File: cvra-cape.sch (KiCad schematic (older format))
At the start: 16 parts

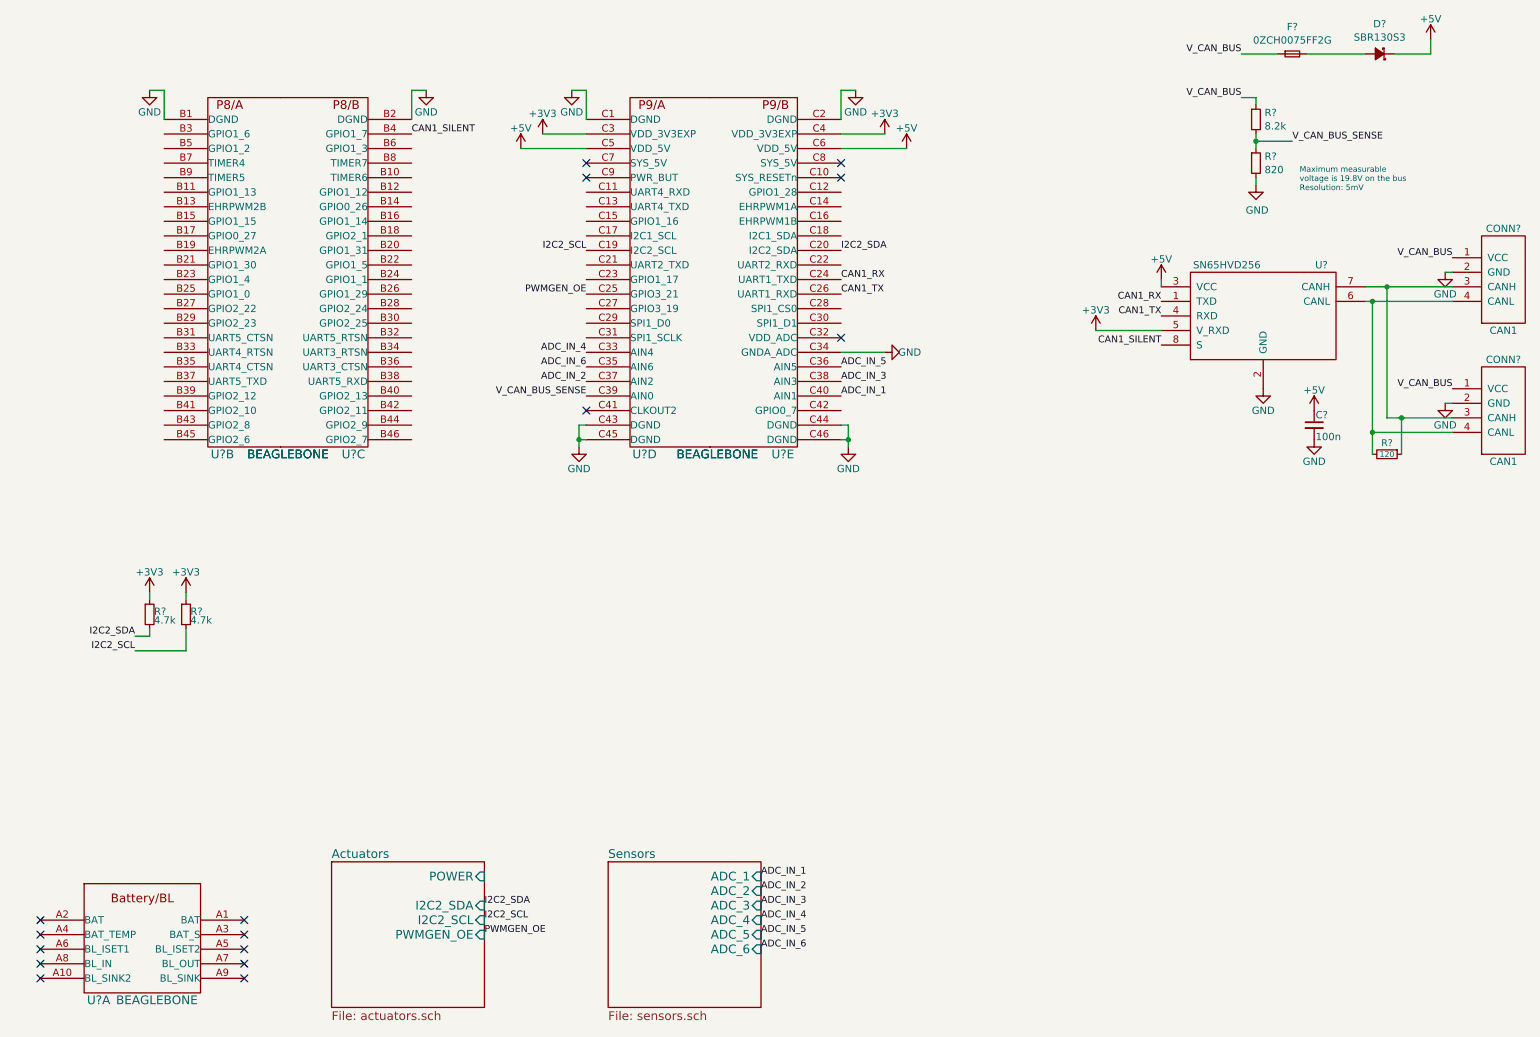
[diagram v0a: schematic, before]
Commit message: Add CAN over SPI interface using MCP251
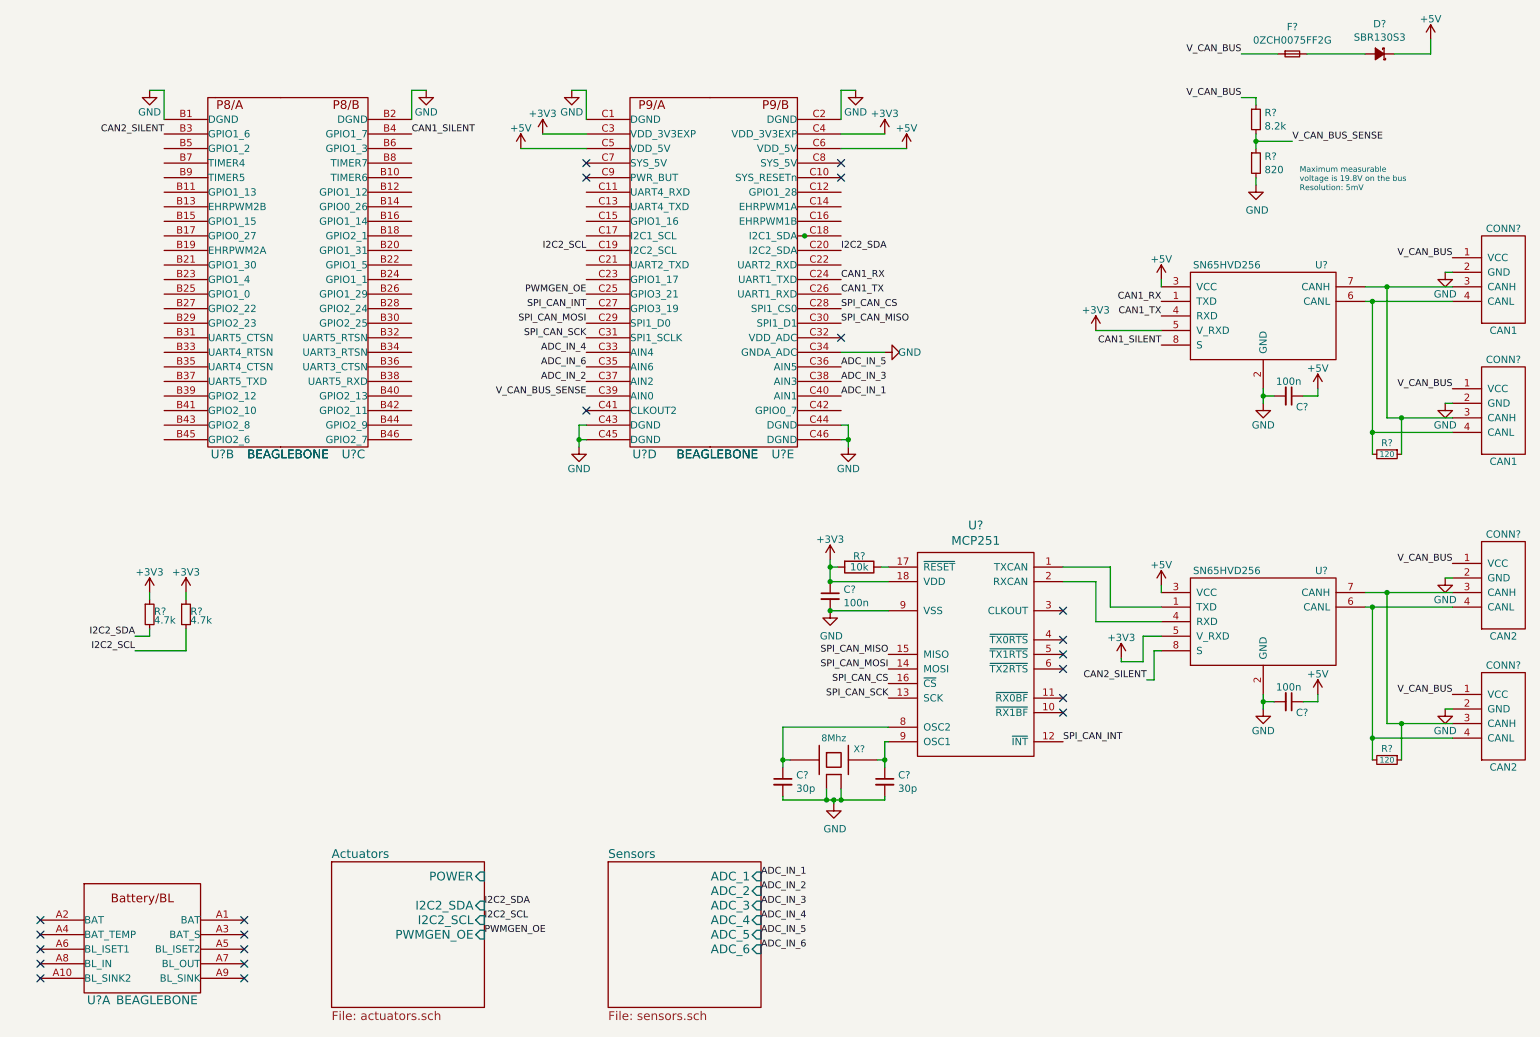
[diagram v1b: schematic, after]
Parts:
- added C? (x2): 30p, symbol C_Small
- added C? (x2): 100n, symbol C_Small
- added CONN? (x2): CAN2, MODULE, symbol CAN
- added R?: 120, symbol R_Small
- added R?: 10k, symbol R
- added U?: SN65HVD256, MODULE, symbol SN65HVD256
- added U?: MCP251, symbol MCP251
- added X?: 8Mhz, symbol XTAL-SMD-4-PADS
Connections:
- net +3V3: now also C?.1, R?.2, U?.18 (VDD), U?.5 (V_RXD)
- net +5V: now also C?.1, U?.3 (VCC)
- net GND: now also C?.2, C?.2, C?.2, C?.2, CONN?.2 (GND), CONN?.2 (GND), CONN?.MECH (GND), CONN?.MECH (GND), U?.2 (GND), U?.9 (VSS), X?.2 (case), X?.4 (case)
- net V_CAN_BUS: now also CONN?.1 (VCC), CONN?.1 (VCC)
- net CAN2_SILENT: now reaches U?.B3 (GPIO1_6)
- net CAN2_SILENT: now also U?.8 (S)
- net SPI_CAN_INT: now reaches U?.C27 (GPIO3_19)
- net SPI_CAN_INT: now also U?.12 (~INT)
- net SPI_CAN_MOSI: now reaches U?.C29 (SPI1_D0)
- net SPI_CAN_MOSI: now also U?.14 (MOSI)
- net SPI_CAN_SCK: now reaches U?.C31 (SPI1_SCLK)
- net SPI_CAN_SCK: now also U?.13 (SCK)
- net SPI_CAN_CS: now reaches U?.C28 (SPI1_CS0)
- net SPI_CAN_CS: now also U?.16 (~CS)
- net SPI_CAN_MISO: now reaches U?.C30 (SPI1_D1)
- net SPI_CAN_MISO: now also U?.15 (MISO)
- new net: U?.1 (TXCAN), U?.1 (TXD)
- new net: U?.2 (RXCAN), U?.4 (RXD)
- new net: CONN?.4 (CANL), CONN?.4 (CANL), R?.2, U?.6 (CANL)
- new net: CONN?.3 (CANH), CONN?.3 (CANH), R?.1, U?.7 (CANH)
- new net: R?.1, U?.17 (~RESET)
- new net: C?.1, U?.8 (OSC2), X?.1
- new net: C?.1, U?.9 (VSS), X?.3
- no-connect marks 16 -> 22
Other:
- moved on the sheet: C?

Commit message: Use 3pin connectors for ADC (with power pin)
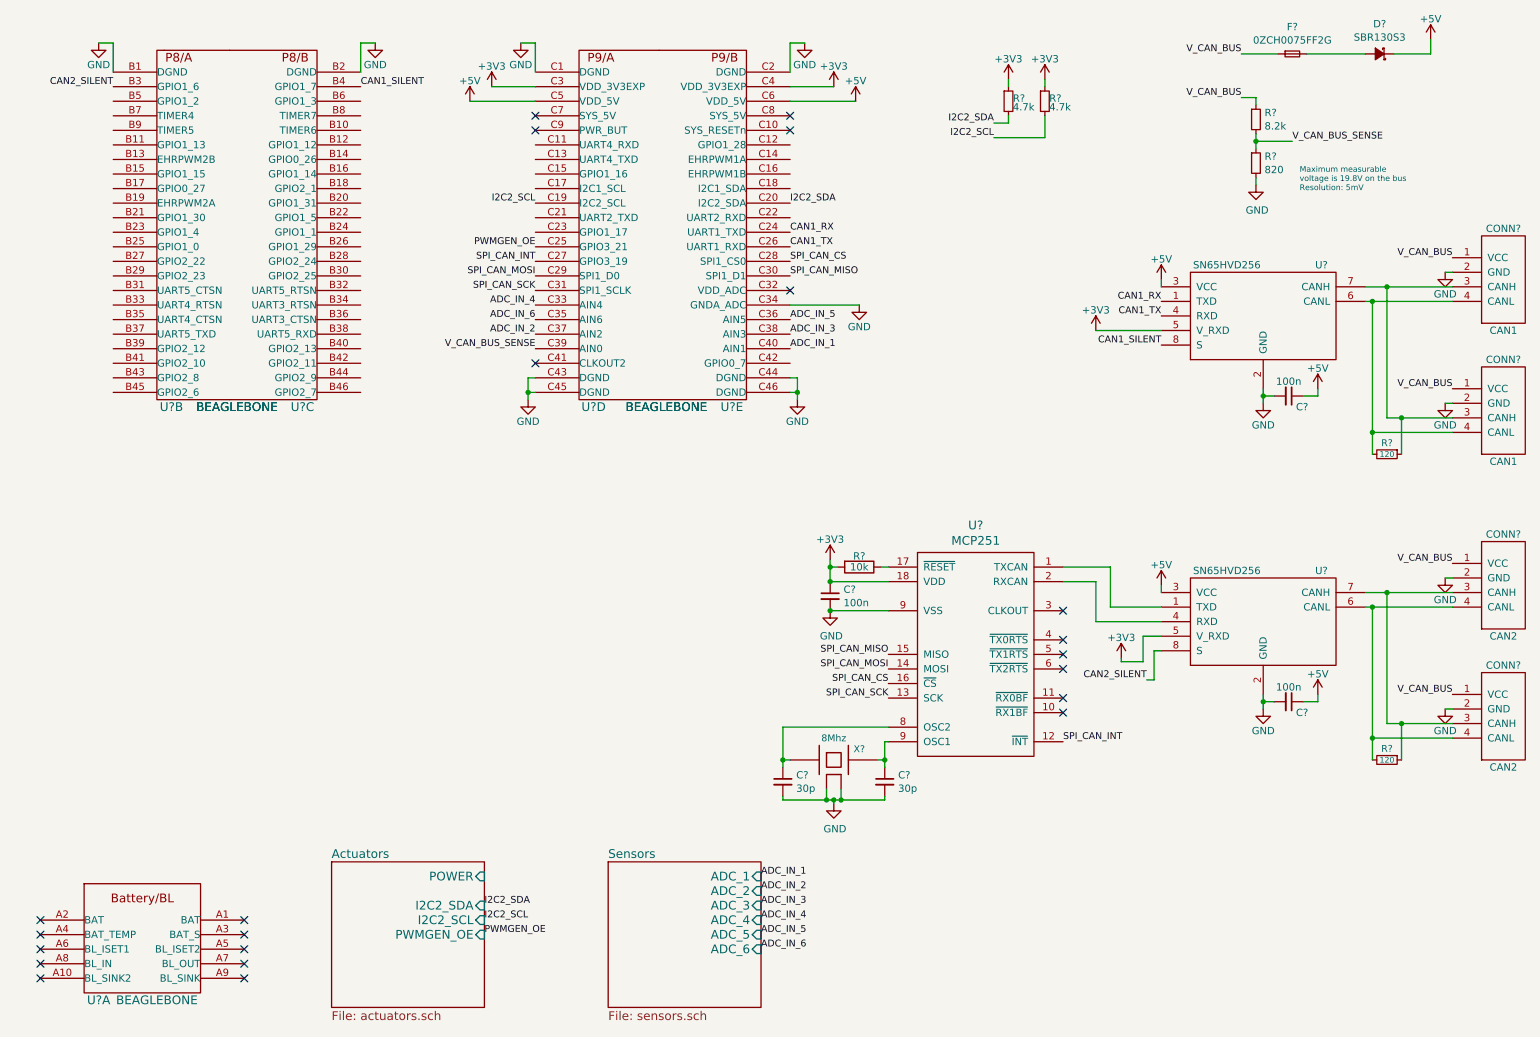
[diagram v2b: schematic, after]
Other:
- moved on the sheet: R?, U?B, U?C, U?D, U?E

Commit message: Add RTC
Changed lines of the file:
@@
 F0 "Actuators" 60
 F1 "actuators.sch" 60
-F2 "I2C2_SDA" I R 3850 6850 60
-F3 "I2C2_SCL" I R 3850 6950 60
-F4 "PWMGEN_OE" I R 3850 7050 60
-F5 "POWER" I R 3850 6650 60
+F2 "I2C2_SDA" I R 3850 6850 47
+F3 "I2C2_SCL" I R 3850 6950 47
+F4 "PWMGEN_OE" I R 3850 7050 47
+F5 "POWER" I R 3850 6650 47
 $EndSheet
 $Comp
@@
 F0 "Sensors" 60
 F1 "sensors.sch" 60
-F2 "ADC_1" I R 5750 6650 60
-F3 "ADC_2" I R 5750 6750 60
-F4 "ADC_3" I R 5750 6850 60
-F5 "ADC_4" I R 5750 6950 60
-F6 "ADC_5" I R 5750 7050 60
-F7 "ADC_6" I R 5750 7150 60
+F2 "ADC_1" I R 5750 6650 47
+F3 "ADC_2" I R 5750 6750 47
+F4 "ADC_3" I R 5750 6850 47
+F5 "ADC_4" I R 5750 6950 47
+F6 "ADC_5" I R 5750 7050 47
+F7 "ADC_6" I R 5750 7150 47
+F8 "I2C_SCL" I R 5750 7350 47
+F9 "I2C_SDA" I R 5750 7250 47
 $EndSheet
 Text Label 5750 6650 0    47   ~ 0
@@
 	1    0    0    -1
 $EndComp
+$Comp
+L +5V #PWR?
+U 1 1 56B4D7F8
+P 4000 6650
+F 0 "#PWR?" H 4000 6500 50  0001 C CNN
+F 1 "+5V" H 4000 6790 50  0000 C CNN
+F 2 "" H 4000 6650 60  0000 C CNN
+F 3 "" H 4000 6650 60  0000 C CNN
+	1    4000 6650
+	1    0    0    -1
+$EndComp
+Wire Wire Line
+	4000 6650 3850 6650
+Text Label 5750 7250 0    47   ~ 0
+I2C2_SDA
+Text Label 5750 7350 0    47   ~ 0
+I2C2_SCL
 $EndSCHEMATC
